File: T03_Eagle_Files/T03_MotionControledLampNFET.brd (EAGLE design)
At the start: 63.5 x 43.2 mm, 30 parts, among them U1 ATMEGA328P-MU, U4 TPS61161ADRVT, X2 16MHz

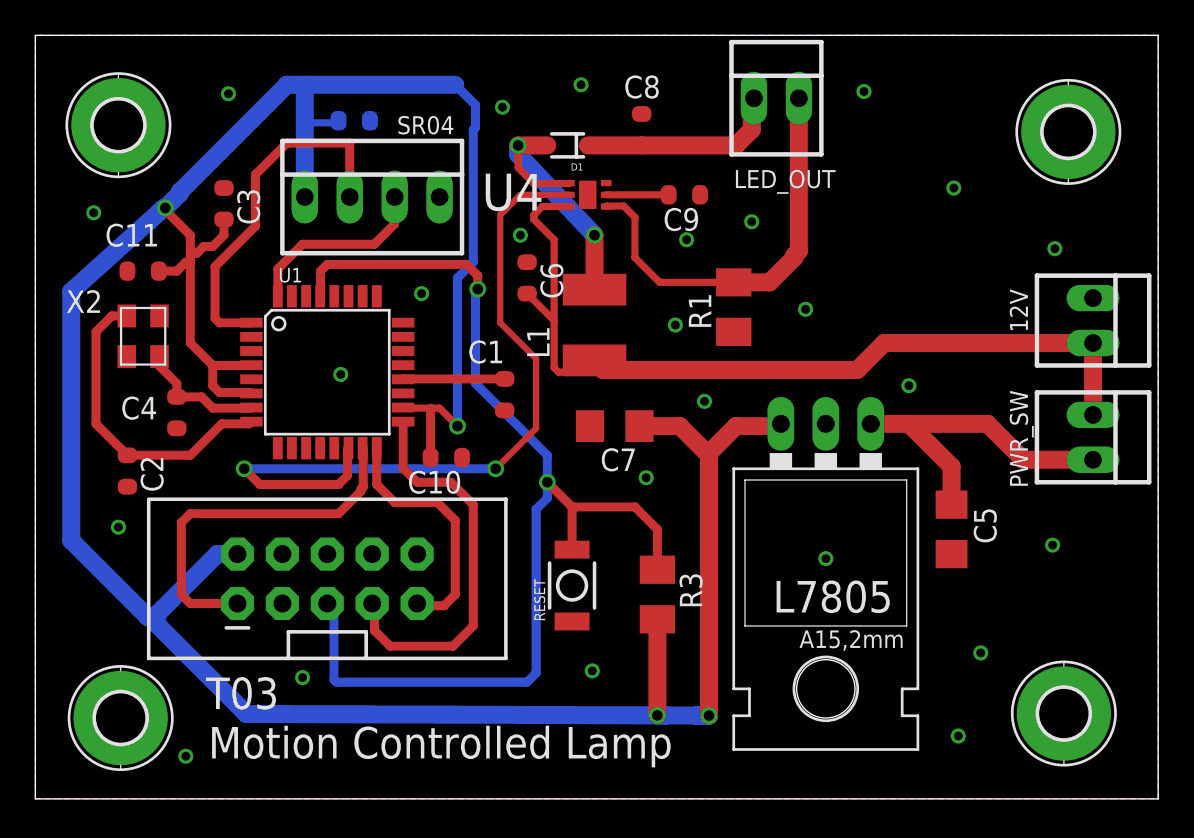
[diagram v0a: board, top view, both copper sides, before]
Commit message: Board Layouts finished, ready for OSH
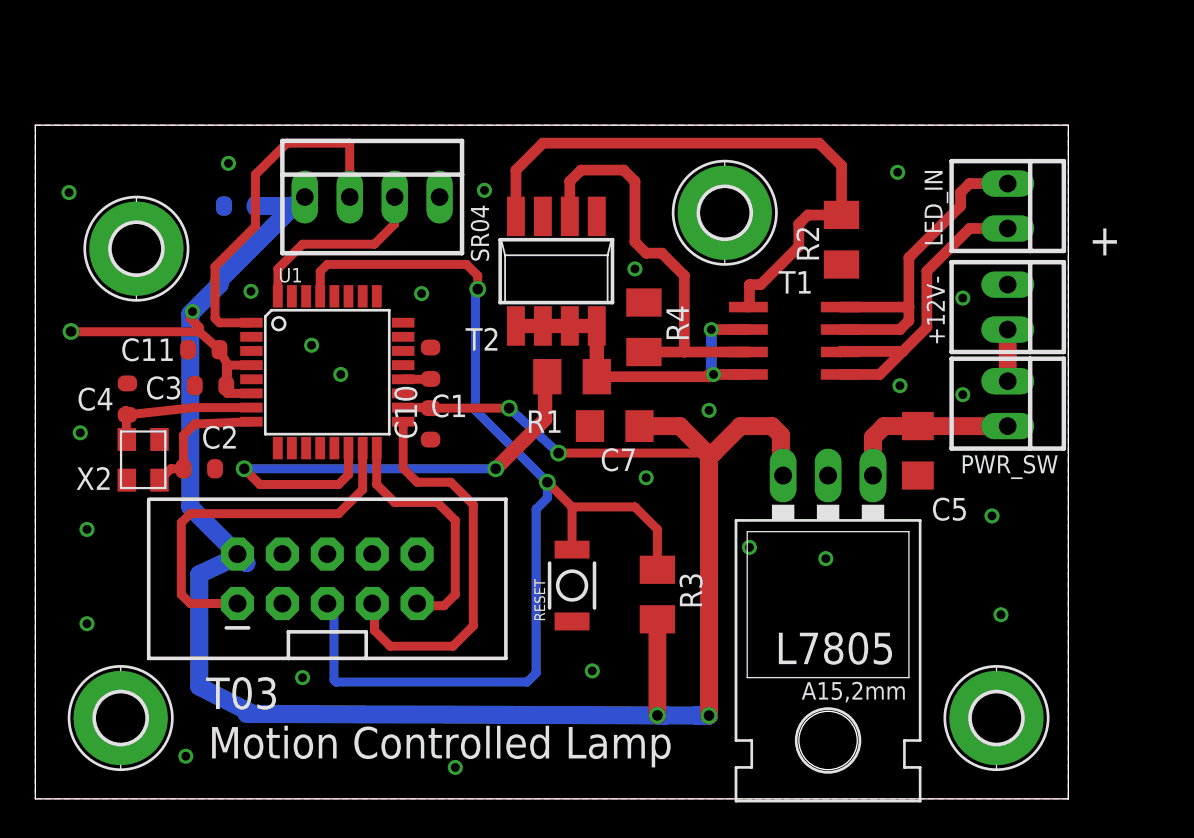
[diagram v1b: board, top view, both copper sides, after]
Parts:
- removed 12V, LED_OUT: 22-23-2021, con-molex:22-23-2021
- removed C6: 1uF, Smartprj:C0603-ROUND
- removed C8: 10uF, Smartprj:C0603-ROUND
- removed C9: 220nF, Smartprj:C0603-ROUND
- removed D1: 0.2V, SparkFun-DiscreteSemi:SOD-323
- removed L1: 22uH, rcl:L4532P
- removed U4: TPS61161ADRVT, Texas Instruments_By_element14_Batch_1:SON65P200X200X80-7N
- added +12V-, LED_IN: 22-23-2021, con-molex:22-23-2021
- added R2, R4: 1.5, rcl:M1206
- added T1: DMN3024LSD, zetex:SO8
- added T2: (no value), zetex:SM8
- R1: value 10 -> 100k
- moved H3 20.0 mm to (39.0, 33.1)
- moved C3 10.3 mm to (9.91, 23.4), turned to 0 degrees
- moved R1 9.96 mm to (30.4, 23.9), turned to 180 degrees
- moved C12 8.08 mm to (11.6, 33.5), turned to 180 degrees
- moved H4 7.06 mm to (5.71, 31.1)
- moved X2 6.98 mm to (6.10, 19.2), turned to 270 degrees
- moved C11 5.61 mm to (9.53, 25.4)
- moved PWR_SW 5.19 mm to (55.0, 22.4)
- moved C5 4.84 mm to (49.9, 19.7)
- moved C1 4.55 mm to (22.4, 24.6), turned to 270 degrees
- moved C2 4.07 mm to (9.27, 18.7), turned to 0 degrees
- moved H2 3.82 mm to (54.4, 4.57)
- moved L7805 2.92 mm to (44.8, 14.5)
- moved C4 2.90 mm to (5.21, 22.6), turned to 90 degrees
- moved C10 2.10 mm to (22.4, 21.2), turned to 90 degrees
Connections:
- removed net +V_BAT: 12V.2, C6.2, L1.1, PWR_SW.1, U4.6
- removed net COMP: C9.2, U4.2
- removed net FB: LED_OUT.2, R1.2, U4.1
- removed net LED_V+: C8.2, D1.C, LED_OUT.1
- removed net SW: D1.A, L1.2, U4.4
- new net +12V: +12V-.2, PWR_SW.1
- new net CURRENT_PROTECT_1: R2.2, T1.1, T2.4
- new net CURRENT_PROTECT_2: R4.2, T1.3, T2.2
- new net LED_ARRAY_1: LED_IN.1, T1.7, T1.8
- new net LED_ARRAY_2: LED_IN.2, T1.5, T1.6
- new net PWM_CTRL_FROM_MC: R1.1, T1.2, T1.4, T2.5, T2.6, T2.7, T2.8
- net GND: now also +12V-.1, R2.1, R4.1, T2.3; no longer 12V.1, C6.1, C8.1, C9.1, R1.1, U4.3, U4.7
- net PWM_LEDS: now also R1.2; no longer U4.5
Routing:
- net +V_BAT: track 49.5 -> 0.00 mm
- net +5V: track 175.4 -> 136.1 mm, vias 4 -> 6
- net CURRENT_PROTECT_1: track 0.00 -> 33.9 mm
- net FB: track 23.5 -> 0.00 mm
- net CURRENT_PROTECT_2: track 0.00 -> 23.4 mm
- net PWM_CTRL_FROM_MC: track 0.00 -> 21.8 mm, vias 0 -> 2
- net LED_ARRAY_1: track 0.00 -> 19.3 mm
- net LED_ARRAY_2: track 0.00 -> 18.3 mm
- net SW: track 16.1 -> 0.00 mm, vias 2 -> 0
- net PWM_LEDS: track 42.7 -> 29.0 mm
- net LED_V+: track 11.5 -> 0.00 mm
- net XTAL2: track 17.6 -> 7.63 mm
- net N$4: track 18.9 -> 10.0 mm
- net AREF: track 5.75 -> 1.56 mm
- net COMP: track 3.53 -> 0.00 mm
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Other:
- board size 63.5 x 43.2 mm -> 58.4 x 38.1 mm
- board text added: "+"
